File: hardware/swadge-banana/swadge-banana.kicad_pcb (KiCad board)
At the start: 2 copper layers, 80.5 x 127.3 mm, 46 parts, among them J1 USB_B_Micro, Q1 Q_NPN_BEC, SW1 SW_SPDT, U1 ESP-13-WROOM-02D, U3 BUS_PCIexpress, U4 QMA6981, U5 AP1117-33, U6 OLED_CONNECTOR

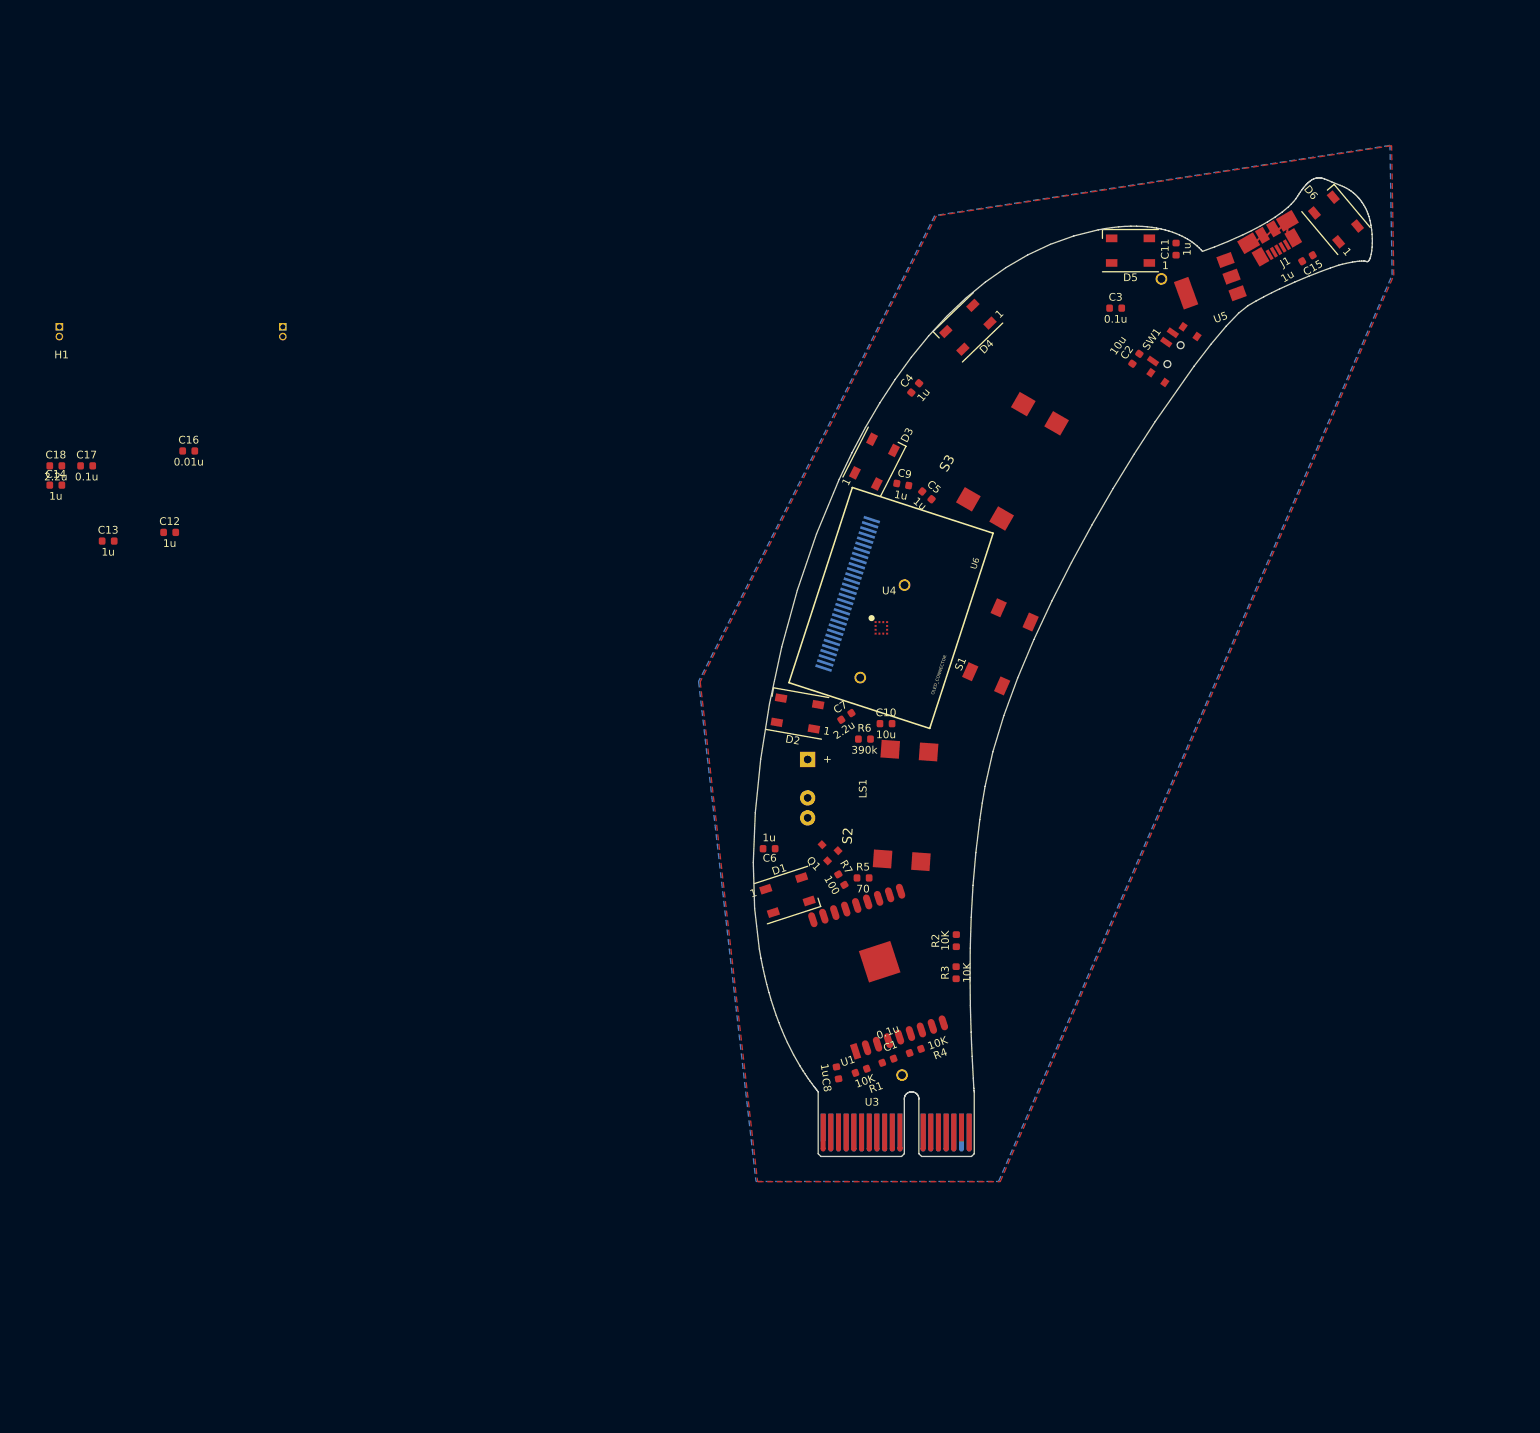
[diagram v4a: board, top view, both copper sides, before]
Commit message: Added 7 inch banana outline
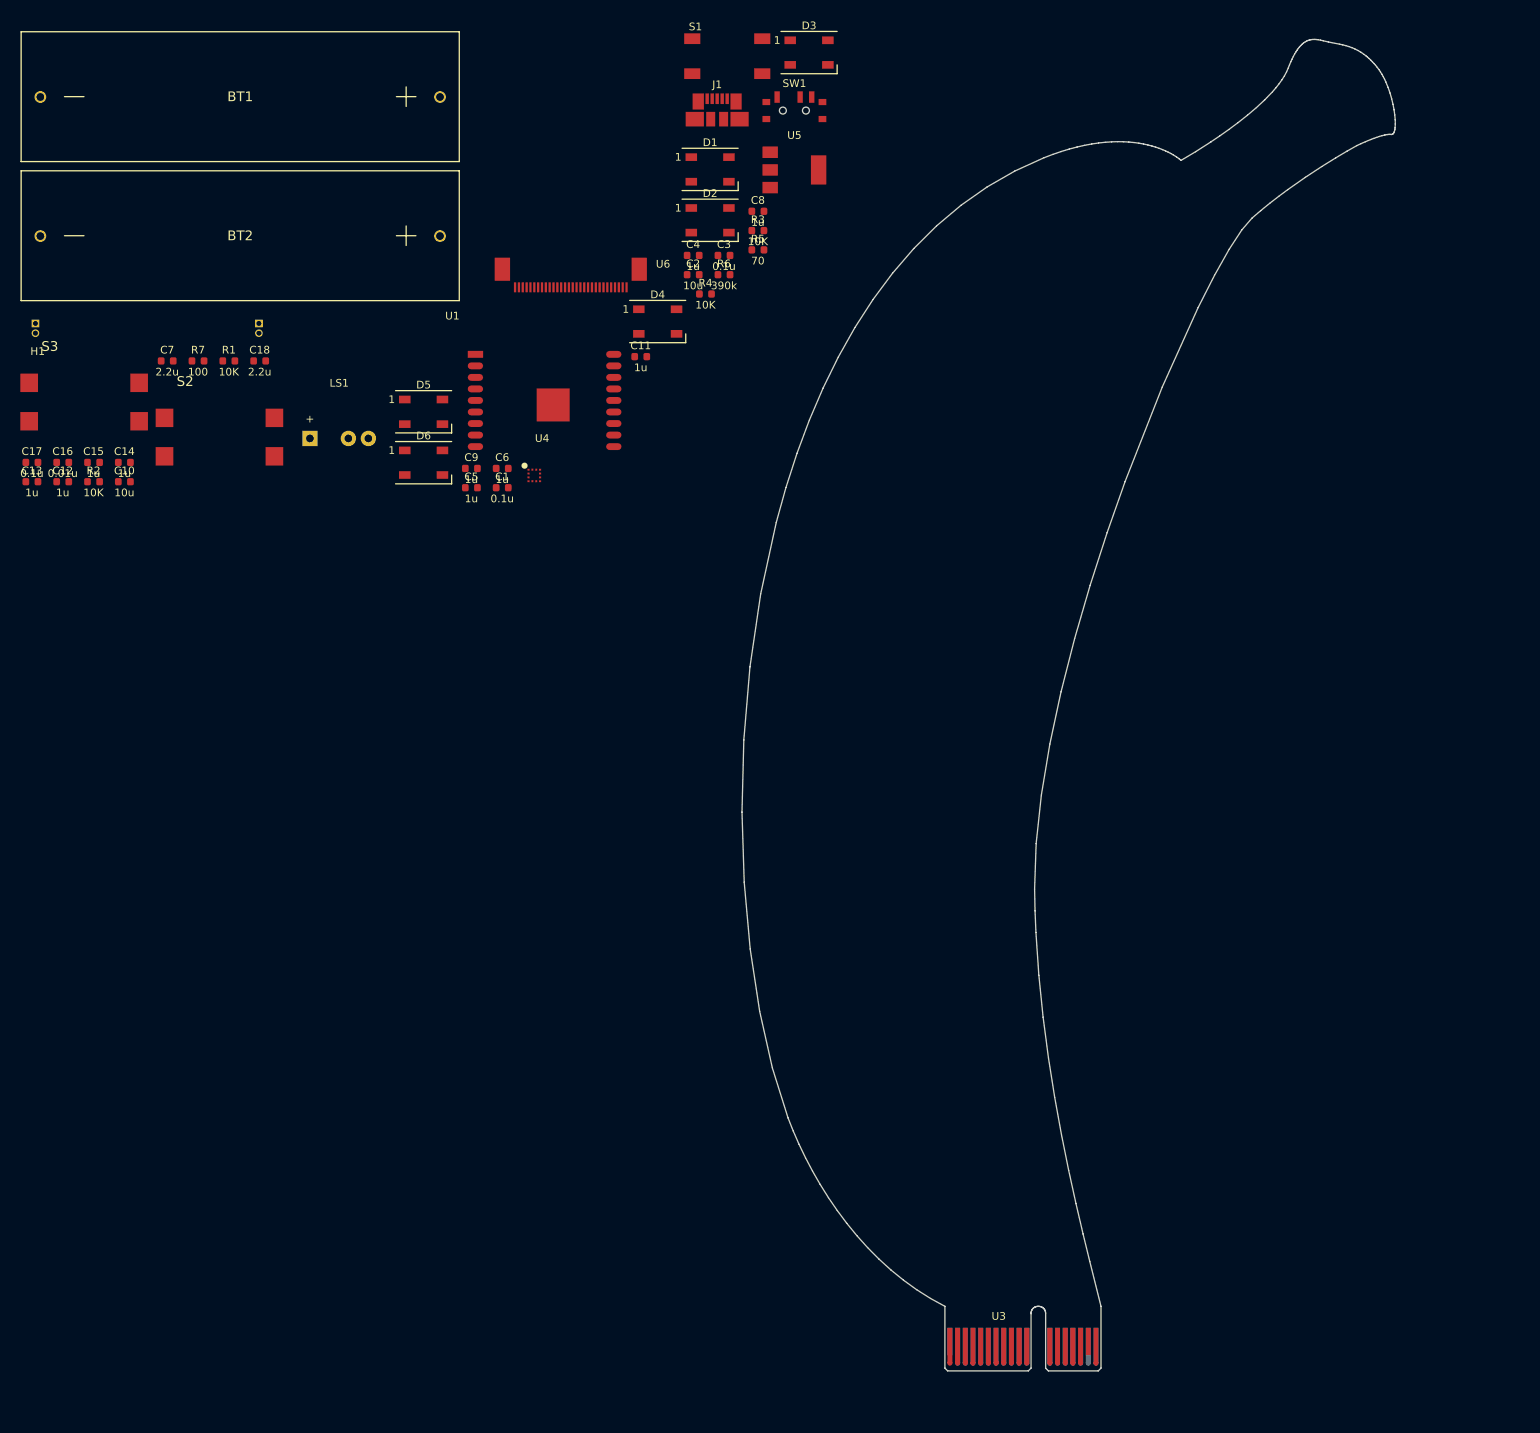
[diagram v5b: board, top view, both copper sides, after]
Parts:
- removed Q1: Q_NPN_BEC, Swadge_Parts:SOT-23
- added U2: OLED_DISPLAY, Swadge_Parts:NULL, F.Cu at (31.5, 70.8)
- BT1, BT2: moved to F.Cu
- U6: footprint Swadge_Parts:microbuilder-UG-2864HSWEG01_0.96IN_WRAPAROUND -> Swadge_Parts:ER-OLED0.96-1.3
- moved C15 160.1 mm to (24.7, 71.3), turned to 0 degrees
- moved BT1 131.3 mm to (43.8, 23.7), turned to 0 degrees
- moved R2 127.1 mm to (24.7, 73.8), turned to 0 degrees
- moved R1 123.7 mm to (42.3, 58.1), turned to 0 degrees
- moved D6 122.8 mm to (67.6, 71.4), turned to 0 degrees
- moved S3 120.4 mm to (24.6, 63.5), turned to 0 degrees
- moved C8 112.6 mm to (111.1, 38.7), turned to 0 degrees
- moved R7 107.5 mm to (38.3, 58.1), turned to 0 degrees
- moved BT2 106.3 mm to (43.8, 41.8), turned to 0 degrees
- moved C10 104.0 mm to (28.7, 73.8)
- moved U1 103.3 mm to (74.4, 57.3), turned to 0 degrees
- moved R4 102.2 mm to (104.3, 49.4), turned to 0 degrees
- moved R3 99.9 mm to (111.1, 41.2), turned to 0 degrees
- moved S2 99.9 mm to (42.2, 68.0), turned to 0 degrees
- moved C7 99.7 mm to (34.3, 58.1), turned to 0 degrees
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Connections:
- LS1 pad 1: +3V3 -> Net-(LS1-Pad1)
- LS1 pad 2: Net-(LS1-Pad2) -> GND
- R7 pad 1: Net-(Q1-Pad1) -> Net-(LS1-Pad1)
- U6 pad 7: Net-(U6-Pad7) -> (no net)
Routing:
- net GND: track 8.78 -> 0.00 mm
- removed copper zone on B.Cu, net GND
- removed copper zone on F.Cu, net GND
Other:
- board size 80.5 x 127.3 mm -> 85 x 173.2 mm
- net class Power removed
- net class Thin removed
- net class xThin removed
- rule pad_to_mask_clearance: 0.2 -> 0.051

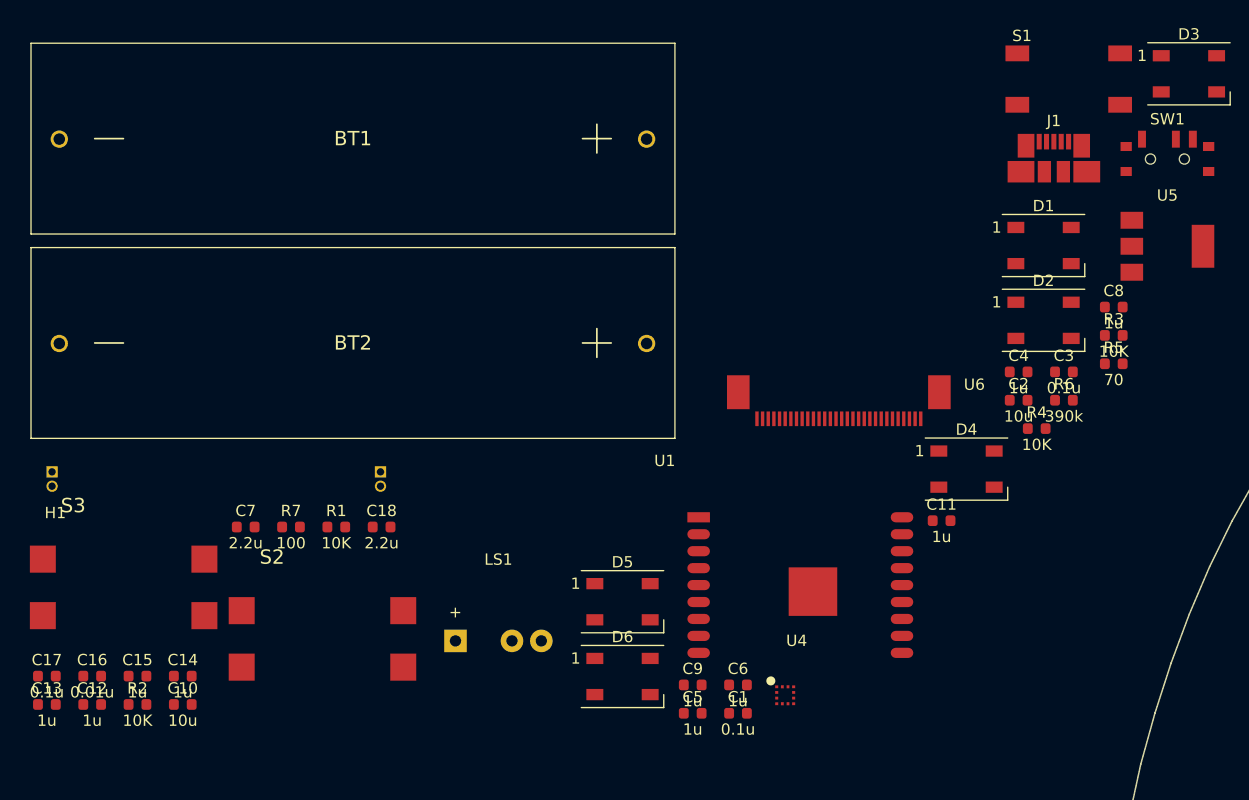
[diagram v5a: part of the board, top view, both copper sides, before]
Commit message: Updated banana sch/pcb from barrel
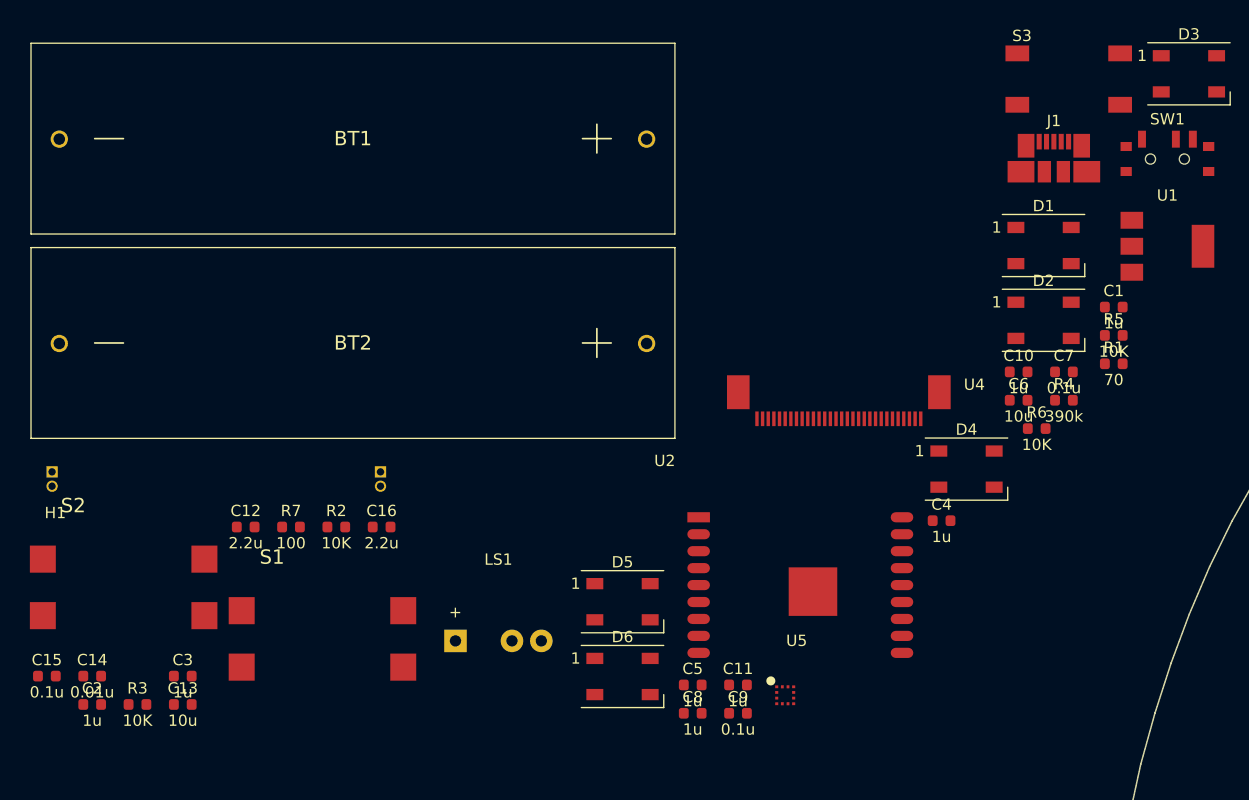
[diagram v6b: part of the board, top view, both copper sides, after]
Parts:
- removed the C13 at (16.7, 73.8)
- removed the C15 at (24.7, 71.3)
- renumbered C8 to C1, C4 to C10, C6 to C11, C7 to C12, C10 to C13, C16 to C14, C17 to C15, C18 to C16, C12 to C2, C14 to C3, C11 to C4, C9 to C5, C2 to C6, C3 to C7, C5 to C8, C1 to C9, R5 to R1, R1 to R2, R2 to R3, R6 to R4, R3 to R5, R4 to R6, S2 to S1, S3 to S2, S1 to S3, U5 to U1, U1 to U2, U6 to U4, U4 to U5, U2 to U6
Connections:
- C4 pad 1: +3V3 -> +5V

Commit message: Merged cnlohr's changes
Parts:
- removed C13: 10u, Swadge_Parts:C_0603_1608Metric
- removed C15: 0.1u, Swadge_Parts:C_0603_1608Metric
- removed the C16 at (46.3, 58.1)
- removed the C7 at (106.7, 44.4)
- removed the C8 at (73.8, 74.6)
- removed the R5 at (111.1, 41.2)
- removed the R6 at (104.3, 49.4)
- removed the U2 at (74.4, 57.3)
- removed the U5 at (82.0, 73.0)
- added C14: 1u, Swadge_Parts:C_0603_1608Metric, F.Cu at (183.7, 28.8)
- added C17: 0.1u, Swadge_Parts:C_0603_1608Metric, F.Cu at (142.8, 38.3)
- added C18: 2.2u, Swadge_Parts:C_0603_1608Metric, F.Cu at (123.9, 79.9)
- added C9: 1u, Swadge_Parts:C_0603_1608Metric, F.Cu at (113.8, 92.0)
- added R2: 10K, Swadge_Parts:R_0603_1608Metric, F.Cu at (120.1, 118.7)
- added R4: 10K, Swadge_Parts:R_0603_1608Metric, F.Cu at (111.4, 99.2)
- added U1: ESP-13-WROOM-02D, Swadge_Parts:ESP-13-WROOM-02, F.Cu at (118.4, 142.6)
- added U6: OLED_CONNECTOR, Swadge_Parts:ER-OLED0.96-1.3, F.Cu at (127.8, 102.3)
- BT1, BT2: moved to B.Cu
- C10: value 1u -> 10u
- C3: value 1u -> 0.1u
- U4: value OLED_CONNECTOR -> QMA6981; footprint Swadge_Parts:ER-OLED0.96-1.3 -> Swadge_Parts:QMA6981
- moved BT1 157.2 mm to (137.8, 149.8), turned to 100 degrees
- moved C3 142.6 mm to (166.2, 33.7), turned to 350 degrees
- moved R1 138.4 mm to (135.0, 160.9), turned to 230 degrees
- moved C8 129.2 mm to (124.3, 167.2), turned to 35 degrees
- moved S3 128.0 mm to (152.2, 72.5), turned to 70 degrees
- moved D6 120.8 mm to (130.8, 174.3), turned to 140 degrees
- moved S2 119.5 mm to (140.6, 135.8), turned to 95 degrees
- moved BT2 111.1 mm to (153.6, 58.9), turned to 62 degrees
- moved H1 109.1 mm to (129.3, 102.6), turned to 80 degrees
- moved D5 105.7 mm to (118.7, 157.3), turned to 113 degrees
- moved C16 103.8 mm to (123.2, 87.3), turned to 345 degrees
- moved C12 101.5 mm to (121.8, 65.9), turned to 340 degrees
- moved C2 101.4 mm to (121.0, 146.7), turned to 170 degrees
- moved R3 101.3 mm to (117.4, 114.6), turned to 40 degrees
- moved C1 91.3 mm to (124.8, 152.9), turned to 100 degrees
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- renumbered C9 to C1, C2 to C12, C14 to C16, C6 to C2, C11 to C6, C12 to C7, C1 to C8, R2 to R1, R1 to R5, R4 to R6, S3 to S1, S1 to S2, S2 to S3, U6 to U2, U1 to U5
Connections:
- C10 pad 2: +3V3 -> Net-(C10-Pad2)
- C3 pad 1: +3V3 -> GND
- C3 pad 2: GND -> +5V
- C4 pad 1: +5V -> GND
- C4 pad 2: GND -> +3V3
- C7 pad 2: Net-(C12-Pad2) -> Net-(C7-Pad2)
- J1 pad 2: (no net) -> Net-(J1-Pad2)
- J1 pad 3: (no net) -> Net-(J1-Pad3)
- J1 pad 4: (no net) -> Net-(J1-Pad4)
- R3 pad 2: SCL -> SDA
- R6 pad 2: Net-(R4-Pad2) -> Net-(R6-Pad2)
- U4 pad 10: GND -> Net-(U4-Pad10)
- U4 pad 11: +3V3 -> Net-(U4-Pad11)
- U4 pad 12: GND -> SCL
- U4 pad 2: Net-(C5-Pad1) -> SDA
- U4 pad 3: Net-(C5-Pad2) -> +3V3
- U4 pad 4: Net-(C8-Pad1) -> GND
- U4 pad 6: +3V3 -> Net-(U4-Pad6)
- U4 pad 7: (no net) -> +3V3
- U4 pad 9: +3V3 -> GND
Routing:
- net GND: track 0.00 -> 686.4 mm, vias 0 -> 38
- net +3V3: track 0.00 -> 614.9 mm, vias 0 -> 10
- net +5V: track 0.00 -> 179.9 mm, vias 0 -> 3
- net SW1: track 0.00 -> 178.7 mm, vias 0 -> 4
- net RX: track 0.00 -> 176.5 mm, vias 0 -> 9
- net SW2: track 0.00 -> 172.4 mm, vias 0 -> 4
- net BZR: track 0.00 -> 168.0 mm, vias 0 -> 7
- net SDA: track 0.00 -> 156.9 mm, vias 0 -> 6
- net SCL: track 0.00 -> 124.8 mm, vias 0 -> 5
- net _RES: track 0.00 -> 122.5 mm, vias 0 -> 4
- net TX: track 0.00 -> 103.9 mm, vias 0 -> 6
- net REST: track 0.00 -> 99.8 mm, vias 0 -> 7
- net SW3: track 0.00 -> 88.3 mm, vias 0 -> 4
- net Net-(BT1-Pad1): track 0.00 -> 86.2 mm
- net ADC_PIN: track 0.00 -> 85.3 mm, vias 0 -> 3
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- added copper zone on B.Cu, net GND
- added copper zone on F.Cu, net GND
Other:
- net class Power added: clearance 0.2, trace_width 0.4, via_dia 0.8, via_drill 0.4

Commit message: Copied schematic from barrel, again Reimported schematic into layout, fixed capacitor changes Fixed one DRC violation
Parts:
- added C4: 1u, Swadge_Parts:C_0603_1608Metric, F.Cu at (166.2, 33.7)
- added H2: Headband, Swadge_Parts:NULL, F.Cu at (103.2, 5.96)
- moved C7 124.0 mm to (120.4, 149.0), turned to 170 degrees
- renumbered C8 to C1, C4 to C10, C6 to C11, C7 to C12, C10 to C13, C16 to C14, C17 to C15, C18 to C16, C12 to C2, C14 to C3, C9 to C5, C2 to C6, C3 to C7, C5 to C8, C1 to C9, R5 to R1, R1 to R2, R2 to R3, R6 to R4, R3 to R5, R4 to R6, S2 to S1, S3 to S2, S1 to S3, U5 to U1, U1 to U2, U6 to U4, U4 to U5, U2 to U6
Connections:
- C7 pad 2: +5V -> +3V3
- J1 pad 2: Net-(J1-Pad2) -> (no net)
- J1 pad 3: Net-(J1-Pad3) -> (no net)
- J1 pad 4: Net-(J1-Pad4) -> (no net)
- U4 pad 7: Net-(U6-Pad7) -> (no net)
- U5 pad 10: Net-(U4-Pad10) -> (no net)
- U5 pad 11: Net-(U4-Pad11) -> (no net)
- U5 pad 5: Net-(U4-Pad5) -> (no net)
- U5 pad 6: Net-(U4-Pad6) -> (no net)
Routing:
- net +3V3: track 614.9 -> 616.8 mm
- net GND: vias 38 -> 43
